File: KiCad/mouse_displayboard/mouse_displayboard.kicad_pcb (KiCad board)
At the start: 2 copper layers, 52.1 x 25.4 mm, 2 parts, among them J1 Conn_01x12_Male, U1 CC56-12EWA

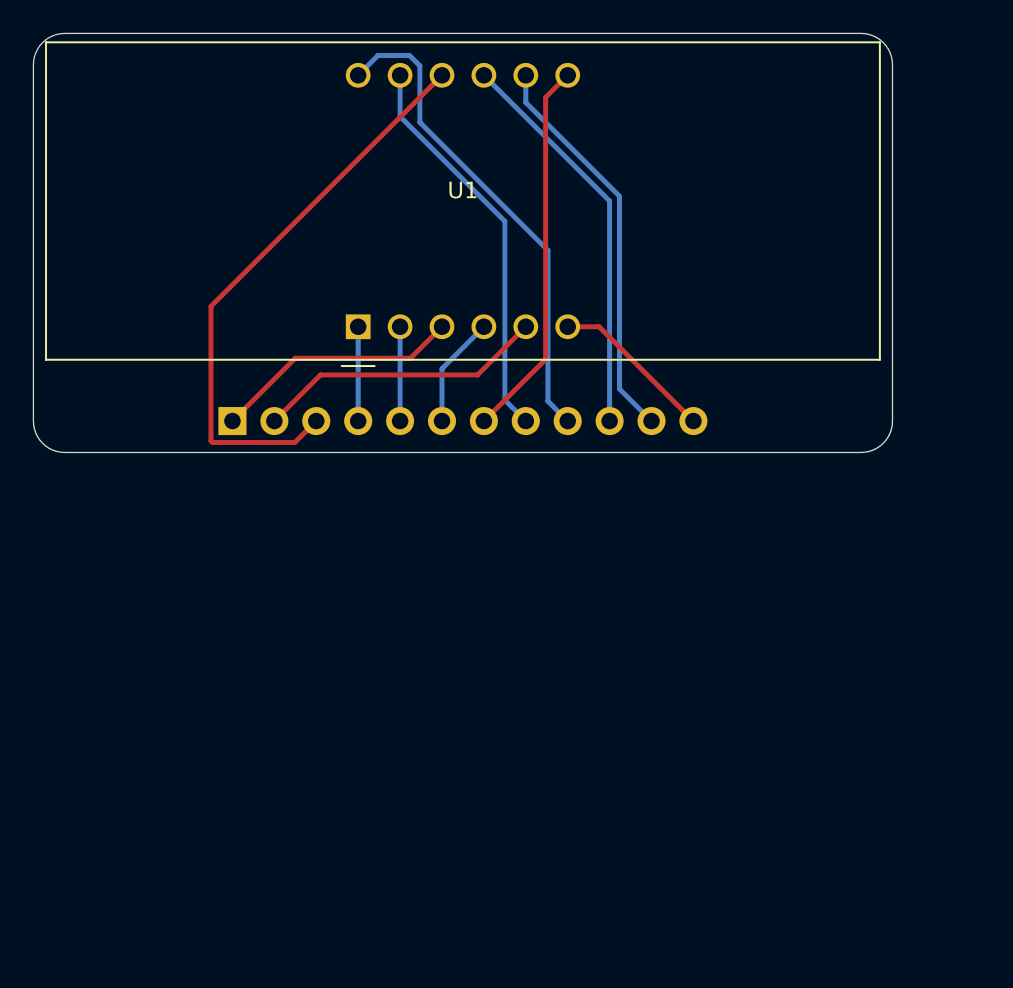
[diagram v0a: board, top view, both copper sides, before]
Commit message: Changed display board and created a new component
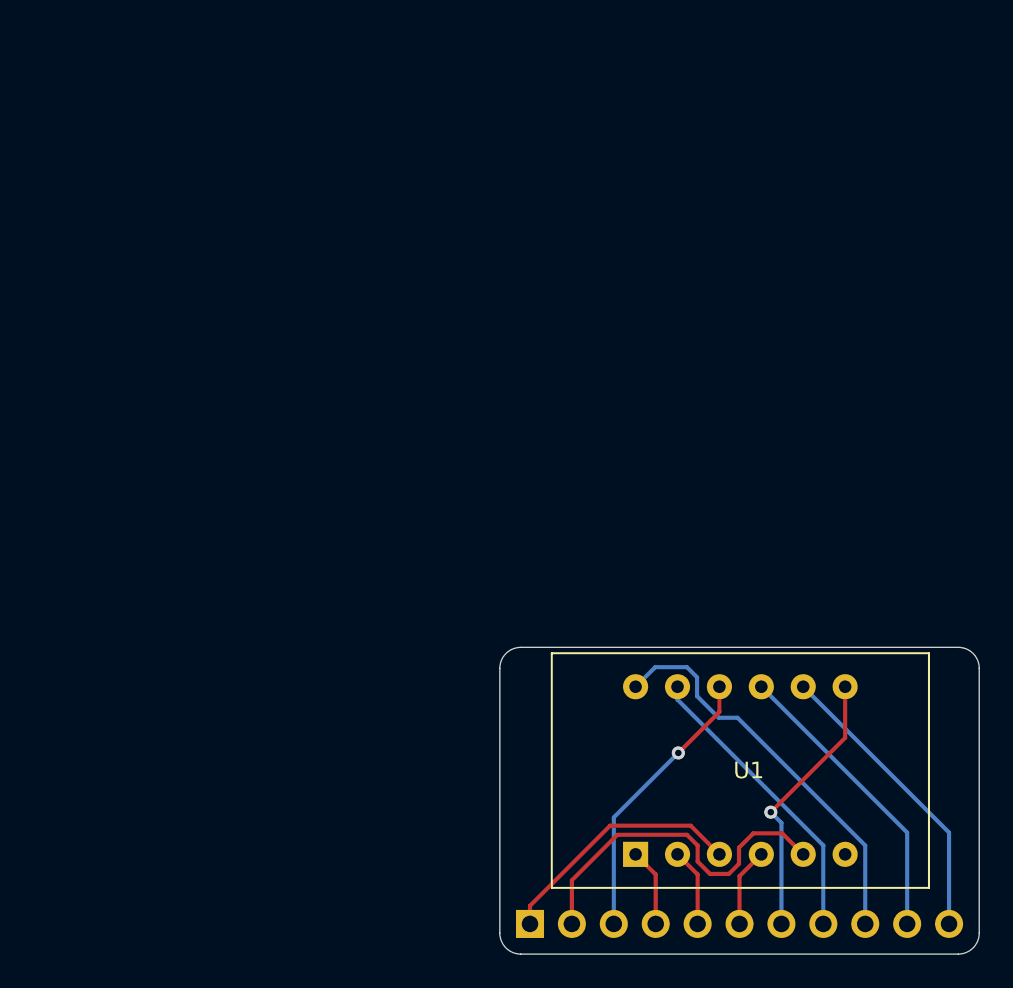
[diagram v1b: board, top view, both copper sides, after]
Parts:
- J1: value Conn_01x12_Male -> Conn_01x11_Male; footprint Connector_PinHeader_2.54mm:PinHeader_1x12_P2.54mm_Vertical -> Connector_PinHeader_2.54mm:PinHeader_1x11_P2.54mm_Vertical
- U1: value CC56-12EWA -> 7_Segment_Display_3_char; footprint Display_7Segment:CA56-12EWA -> e7020e_custom_footprint_lib:7 Segment Display 3 char
- moved J1 35.4 mm to (141.2, 113.0)
- moved U1 27.5 mm to (147.6, 98.7), turned to 0 degrees
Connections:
- U1 pad 6: Net-(J1-Pad12) -> (no net)
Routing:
- net f: track 34.9 -> 17.0 mm, vias 0 -> 1
- net Net-(J1-Pad12): track 9.99 -> 0.00 mm
- net b: track 23.1 -> 16.5 mm, vias 0 -> 1
- net a: track 24.1 -> 18.0 mm
- net Net-(J1-Pad11): track 24.1 -> 18.0 mm
- net Net-(J1-Pad10): track 24.1 -> 18.0 mm
- net Net-(J1-Pad9): track 29.7 -> 24.3 mm
- net g: track 17.6 -> 21.5 mm
- net c: track 6.77 -> 4.76 mm
- net d: track 5.72 -> 4.72 mm
- net e: track 5.72 -> 4.72 mm
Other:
- board size 52.1 x 25.4 mm -> 29.1 x 18.6 mm

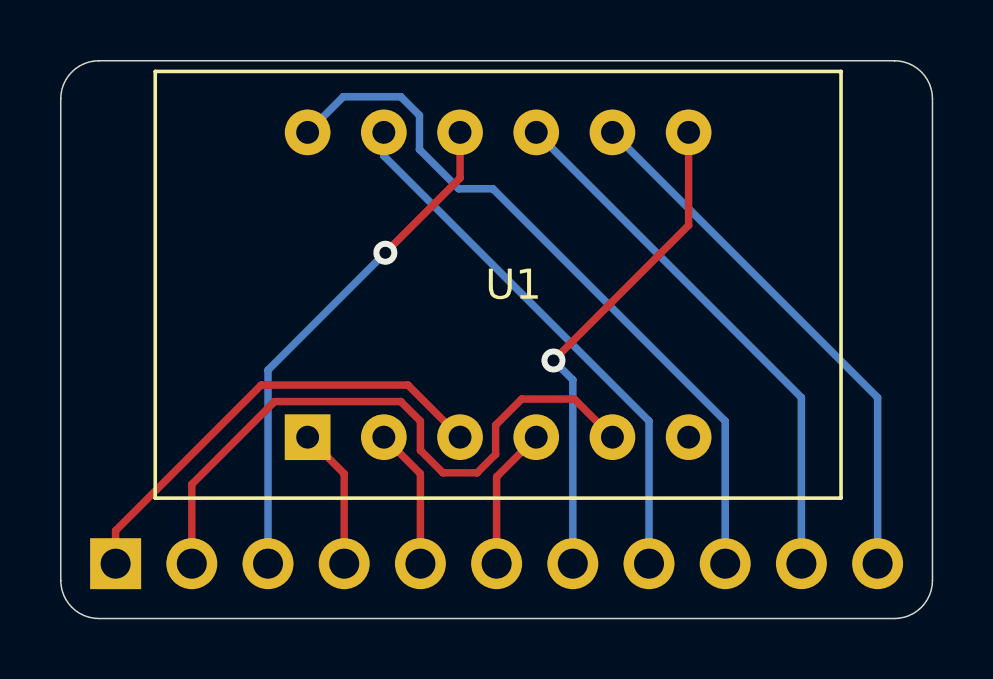
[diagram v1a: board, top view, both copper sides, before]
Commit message: Added resistors for display-board
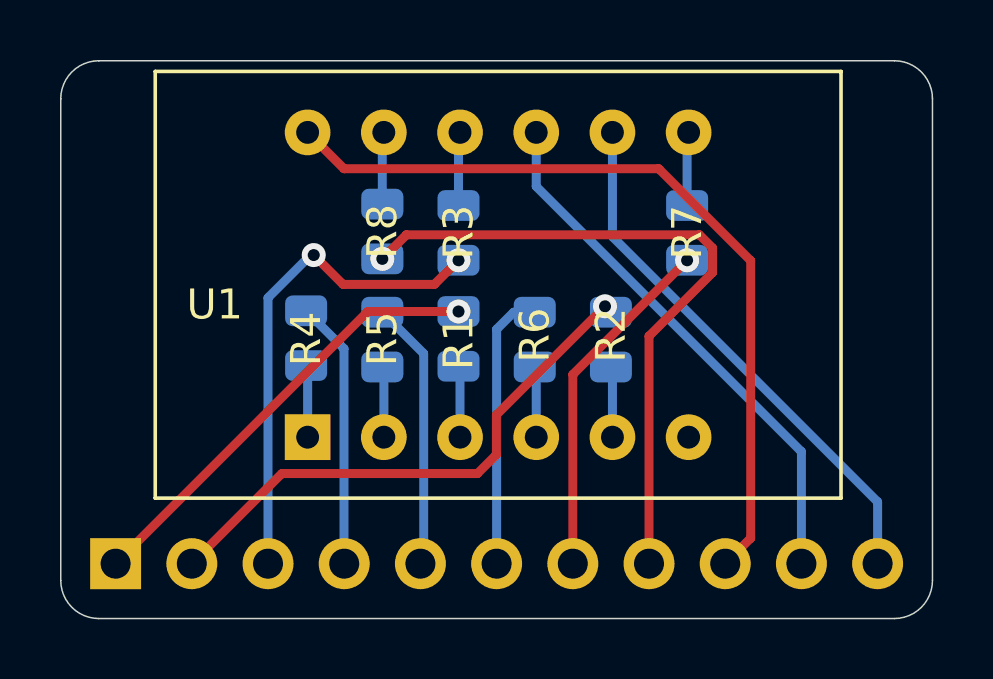
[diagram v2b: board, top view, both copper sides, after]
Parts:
- added R1: 220R, Resistor_SMD:R_0805_2012Metric, B.Cu at (152.7, 105.5)
- added R2: 220R, Resistor_SMD:R_0805_2012Metric, B.Cu at (157.7, 105.6)
- added R3: 220R, Resistor_SMD:R_0805_2012Metric, B.Cu at (152.7, 102.0)
- added R4: 220R, Resistor_SMD:R_0805_2012Metric, B.Cu at (147.6, 105.5)
- added R5: 220R, Resistor_SMD:R_0805_2012Metric, B.Cu at (150.1, 105.6)
- added R6: 220R, Resistor_SMD:R_0805_2012Metric, B.Cu at (155.2, 105.6)
- added R7: 220R, Resistor_SMD:R_0805_2012Metric, B.Cu at (160.3, 102.0)
- added R8: 220R, Resistor_SMD:R_0805_2012Metric, B.Cu at (150.1, 102.0)
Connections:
- J1 pad 1: dpx -> Net-(J1-Pad1)
- J1 pad 2: g -> Net-(J1-Pad2)
- J1 pad 3: f -> Net-(J1-Pad3)
- J1 pad 4: e -> Net-(J1-Pad4)
- J1 pad 5: d -> Net-(J1-Pad5)
- J1 pad 6: c -> Net-(J1-Pad6)
- J1 pad 7: b -> Net-(J1-Pad7)
- J1 pad 8: a -> Net-(J1-Pad8)
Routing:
- net Net-(J1-Pad8): track 0.00 -> 22.9 mm, vias 0 -> 1
- net g: track 21.5 -> 2.36 mm
- net Net-(J1-Pad2): track 0.00 -> 18.1 mm, vias 0 -> 1
- net Net-(J1-Pad3): track 0.00 -> 16.5 mm, vias 0 -> 2
- net a: track 18.0 -> 2.41 mm
- net Net-(J1-Pad1): track 0.00 -> 14.9 mm, vias 0 -> 1
- net f: track 17.0 -> 2.46 mm, vias 1 -> 0
- net b: track 16.5 -> 2.46 mm, vias 1 -> 0
- net dpx: track 15.3 -> 2.39 mm
- net Net-(J1-Pad7): track 0.00 -> 11.7 mm, vias 0 -> 1
- net Net-(J1-Pad6): track 0.00 -> 9.32 mm
- net Net-(J1-Pad5): track 0.00 -> 9.00 mm
- net Net-(J1-Pad4): track 0.00 -> 8.96 mm
- net Net-(J1-Pad9): track 24.3 -> 27.0 mm
- net c: track 4.76 -> 2.36 mm
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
